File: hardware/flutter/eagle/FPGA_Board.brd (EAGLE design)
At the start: 100 x 77 mm, 45 parts, among them IC1 AT45DB161D-SU, IC2 MEGA8-AI, IC3 MAX3468CSA, Q1 8Mhz, U2 XC3S50AVQ100

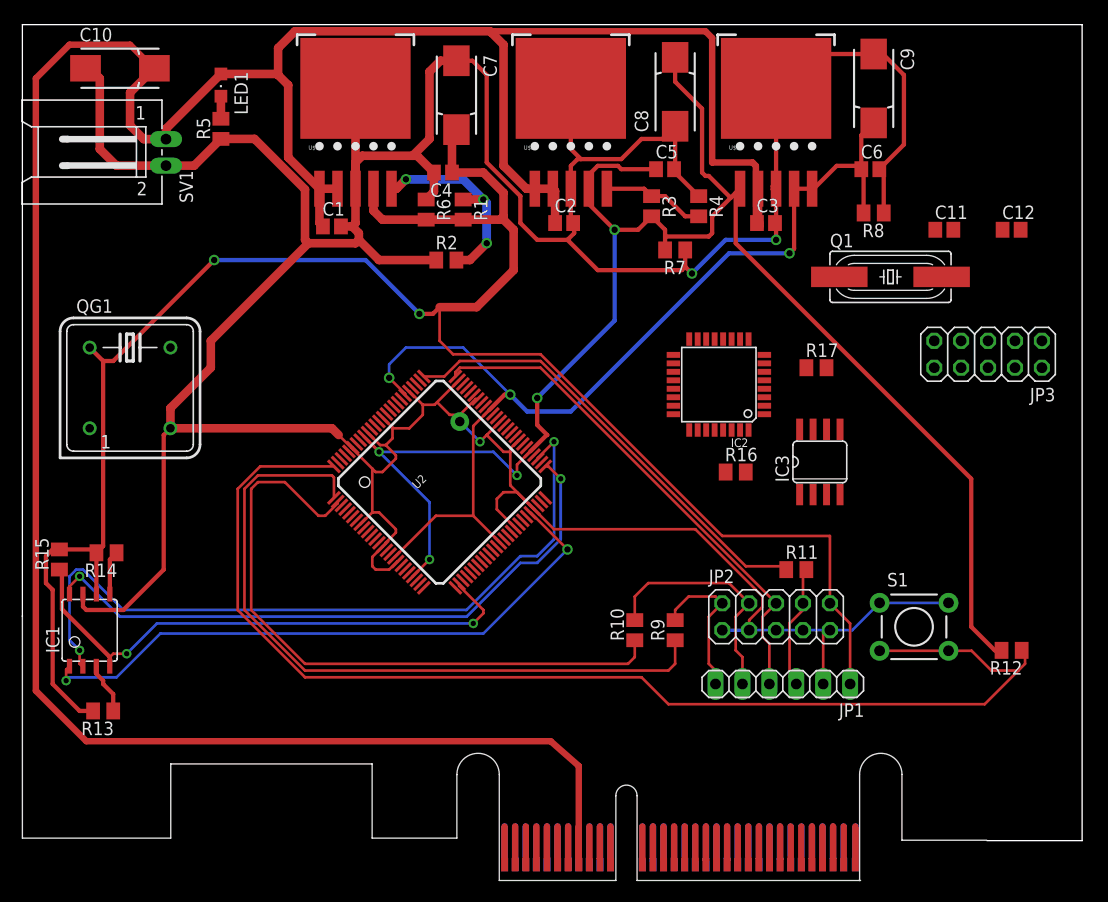
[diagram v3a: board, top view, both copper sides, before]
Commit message: organized parts of schematic by function finished routing, some power pins are not connected
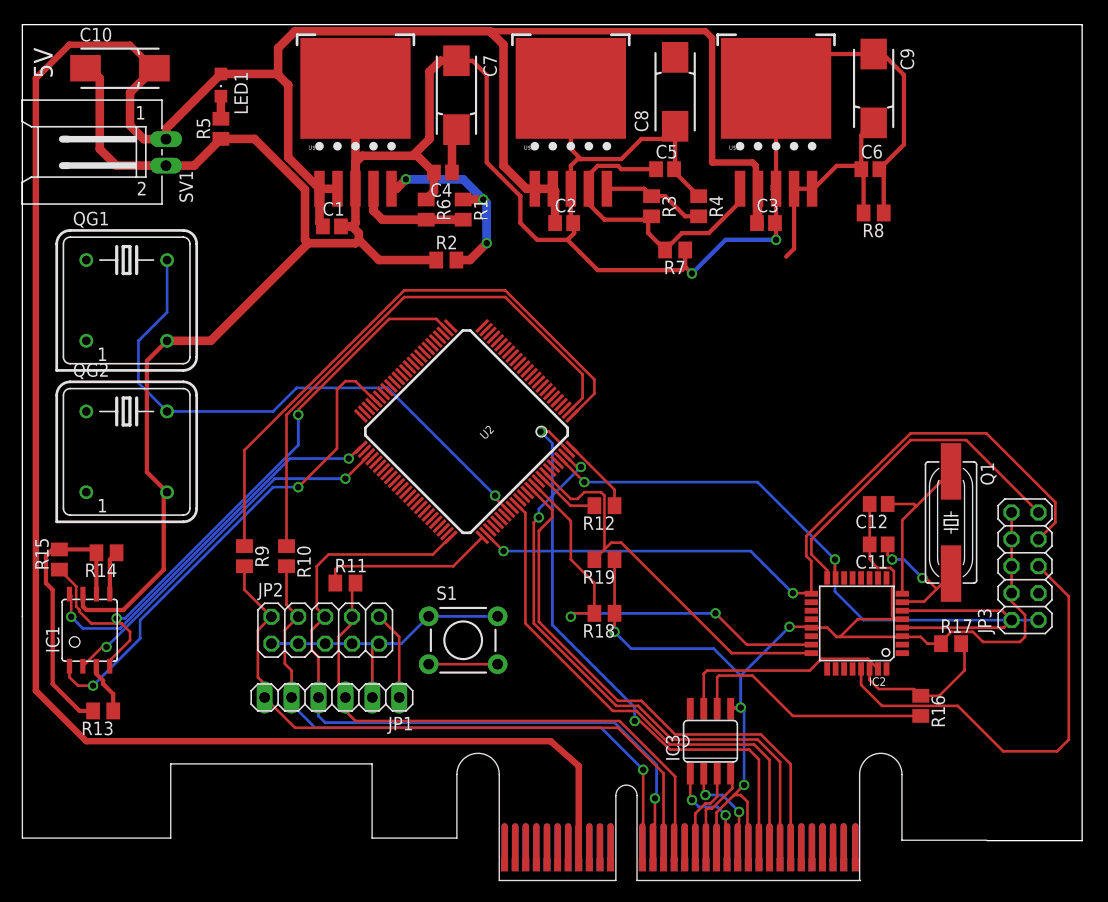
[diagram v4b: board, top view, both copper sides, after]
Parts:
- added QG2: (no value), crystal:DIL08S
- added R18, R19: 10k, resistor:M0805
- moved JP2 42.6 mm to (28.6, 22.9)
- moved R11 42.6 mm to (30.5, 27.3)
- moved S1 42.6 mm to (41.6, 21.9)
- moved JP1 42.6 mm to (29.2, 16.5)
- moved R9 41.2 mm to (21.0, 29.8), turned to 270 degrees
- moved R12 40.8 mm to (54.9, 34.6)
- moved R10 33.6 mm to (24.9, 29.8), turned to 270 degrees
- moved C11 30.3 mm to (80.8, 31.0), turned to 180 degrees
- moved R17 29.0 mm to (87.6, 21.6)
- moved C12 28.8 mm to (80.8, 34.8), turned to 180 degrees
- moved IC3 28.3 mm to (64.9, 12.4)
- moved R16 28.1 mm to (84.8, 15.7), turned to 270 degrees
- moved IC2 26.0 mm to (78.7, 23.5)
- moved Q1 23.9 mm to (87.6, 33.0), turned to 270 degrees
- moved JP3 20.3 mm to (94.6, 28.9), turned to 90 degrees
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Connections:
- removed net CLOCK: QG1.5
- new net FPGA_SPI_CLOCK: QG1.5, QG2.5, U2.P83
- new net N$13: U$4.A01(PRSNT1), U$4.A32(PRSNT2)
- new net TIMING_RESET: IC2.24, R19.2, U2.P93
- new net UC_FPGA_SPI_CS: IC2.23, R18.2, U2.P90
- new net UC_MISO: IC2.16, JP3.9
- new net UC_MOSI: IC2.15, JP3.1, U2.P97
- new net UC_RESET: IC2.29, JP3.5
- new net UC_SCK: IC2.17, JP3.7, U2.P77
- net GND: now also JP3.10, JP3.4, JP3.6, JP3.8, QG2.4, R18.1, R19.1
- net SLOWCLK/CLK: now also U2.P85
- net SLOWCLK/CS: now also U2.P98
- net SLOWCLK/MOSI: now also U2.P99
- net VCC3.3: now also JP3.2, QG2.8
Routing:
- net VCC2.5: track 160.6 -> 36.1 mm, vias 5 -> 0
- net VCC3.3: track 187.6 -> 71.1 mm, vias 2 -> 0
- net PROG_B: track 116.2 -> 13.7 mm
- net VCC1.2: track 99.6 -> 23.5 mm, vias 3 -> 0
- net UC_SCK: track 0.00 -> 73.0 mm, vias 0 -> 2
- net SLOWCLK/MOSI: track 0.00 -> 57.6 mm, vias 0 -> 2
- net SLOWCLK/CS: track 0.00 -> 56.9 mm, vias 0 -> 2
- net UC_MOSI: track 0.00 -> 54.9 mm, vias 0 -> 2
- net FPGA_SPI_CLOCK: track 0.00 -> 54.6 mm, vias 0 -> 1
- net PPS: track 0.00 -> 52.7 mm
- net SLOWCLK/CLK: track 0.00 -> 49.9 mm
- net TMS: track 14.6 -> 63.4 mm
- net TCK: track 12.2 -> 55.5 mm
- net UC_RESET: track 0.00 -> 41.7 mm
- net UC_FPGA_SPI_CS: track 0.00 -> 40.9 mm, vias 0 -> 2
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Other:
- board text added: "5V"

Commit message: connected all the signals to wires just gps module is missing on the board
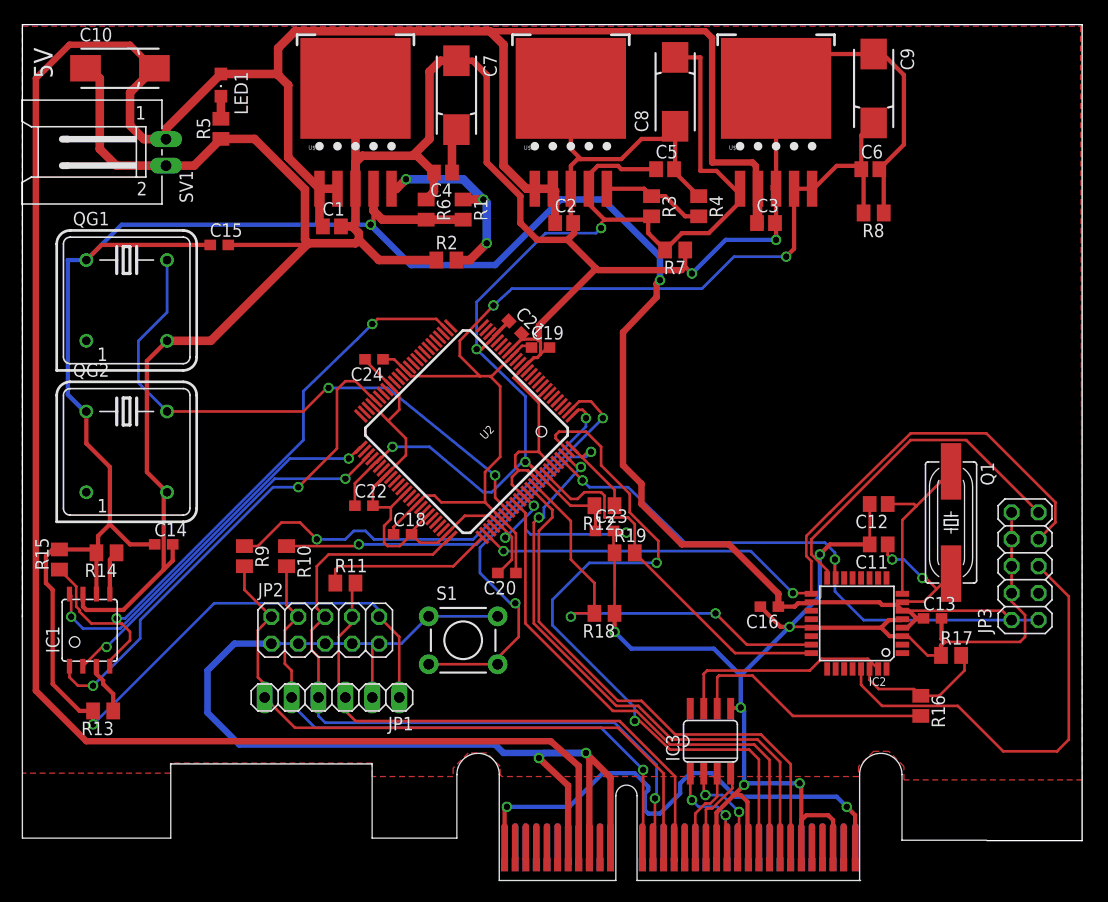
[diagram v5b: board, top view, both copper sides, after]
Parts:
- added C13, C14, C15, C16, C18, C19, C20, C21, C22, C23, C24: (no value), resistor:C0603
- moved R19 2.01 mm to (56.8, 30.2), turned to 0 degrees
- moved R17 1.11 mm to (87.6, 20.5)
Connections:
- removed net AVCC: IC2.18
- net GND: now also C13.2, C14.2, C15.2, C16.2, C18.2, C19.2, C20.2, C21.2, C22.2, C23.2, C24.2
- net VCC1.2: now also C18.1, C19.1, C20.1, C24.1
- net VCC2.5: now also C21.1, C22.1, C23.1
- net VCC3.3: now also C13.1, C14.1, C15.1, C16.1, IC2.18
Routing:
- net GND: track 409.1 -> 647.4 mm, vias 6 -> 13
- net VCC3.3: track 71.1 -> 273.7 mm, vias 0 -> 3
- net VCC2.5: track 36.1 -> 124.0 mm, vias 0 -> 4
- net VCC1.2: track 23.5 -> 109.7 mm, vias 0 -> 2
- net N$13: track 0.00 -> 51.5 mm, vias 0 -> 2
- net PROG_B: track 13.7 -> 42.5 mm, vias 0 -> 2
- net N$4: track 56.1 -> 41.8 mm, vias 0 -> 2
- net N$2: track 52.1 -> 39.4 mm, vias 0 -> 2
- net SLOWCLK/MOSI: track 57.6 -> 69.5 mm
- net TIMING_RESET: track 37.5 -> 35.4 mm
- net N$9: track 14.3 -> 13.2 mm
- net CS_EEPROM: track 60.1 -> 60.8 mm
- net FPGA_SPI_CLOCK: track 54.6 -> 55.2 mm, vias 1 -> 2
- added copper zone on layer 1, net N$14

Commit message: applied changed in hgg.lbr to the board, added ground planes
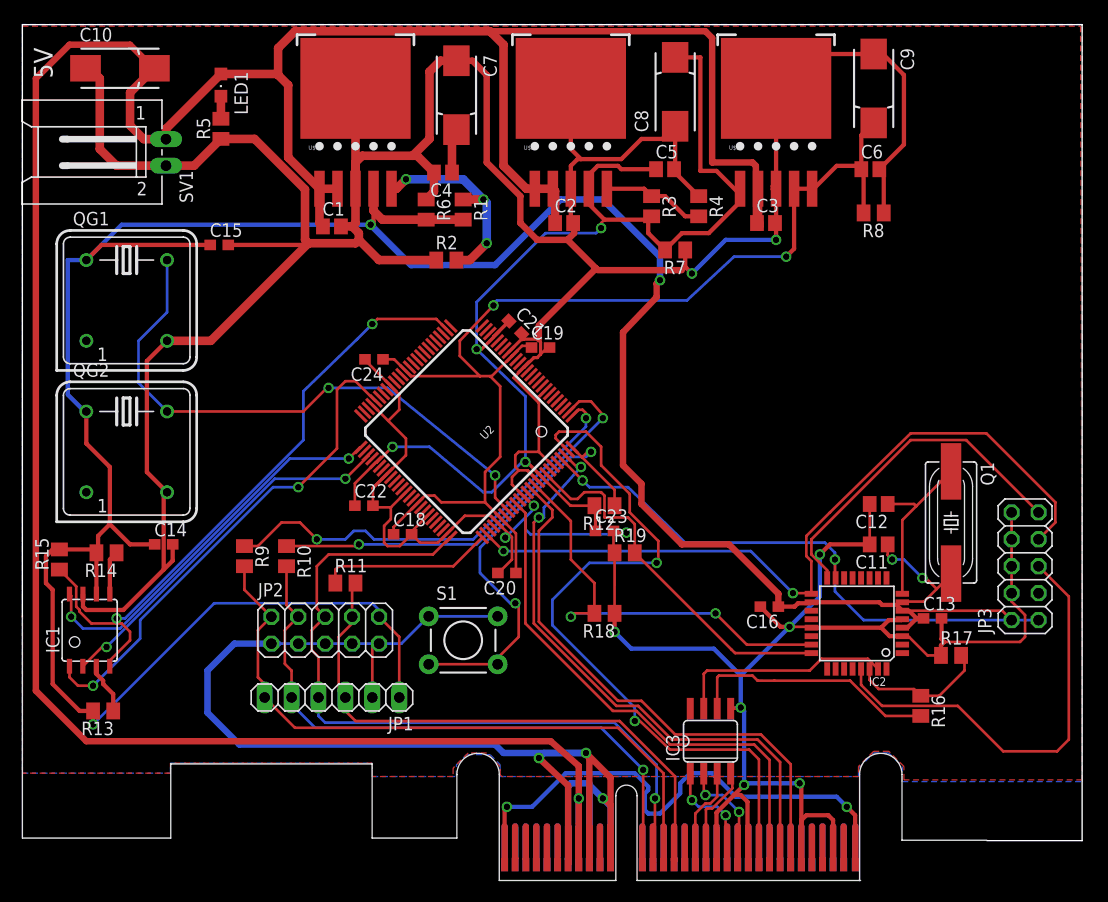
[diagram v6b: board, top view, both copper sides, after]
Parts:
- added U$5: HGG_LOGO, hgg:HGG_LOGO
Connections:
- net +5V: now also U$4.B08(+5V)
- net GND: now also U$4.B07(GND), U$4.B09(GND), U$4.B11(GND)
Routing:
- net GND: track 647.4 -> 681.4 mm, vias 13 -> 14
- net +5V: track 268.5 -> 274.7 mm, vias 0 -> 1
- added copper zone on layer 1, net GND
- added copper zone on layer 16, net GND
- removed copper zone on layer 1, net N$14
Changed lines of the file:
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@@
 <element name="C23" library="resistor" package="C0603" value="" x="54.9275" y="32.22625"/>
 <element name="C24" library="resistor" package="C0603" value="" x="33.17875" y="48.41875" rot="R180"/>
+<element name="U$5" library="hgg" package="HGG_LOGO" value="HGG_LOGO" x="90.17" y="70.96125"/>
 </elements>
 <signals>
@@
 <wire x1="53.49875" y1="10.795" x2="53.49875" y2="0.74125" width="0.6096" layer="1"/>
 <wire x1="53.49875" y1="0.74125" x2="53.5" y2="0.74" width="0.6096" layer="1"/>
-<wire x1="55.5" y1="0.74" x2="55.5" y2="8.9525" width="0.6096" layer="1"/>
+<wire x1="55.5" y1="0.74" x2="55.5" y2="6.35" width="0.6096" layer="1"/>
+<wire x1="55.5" y1="6.35" x2="55.5" y2="8.9525" width="0.6096" layer="1"/>
 <wire x1="55.5" y1="8.9525" x2="53.18125" y2="11.27125" width="0.6096" layer="1"/>
 <via x="53.18125" y="11.27125" extent="1-16" drill="0.6" shape="square"/>
@@
 <wire x1="17.4625" y1="19.05" x2="20.0025" y2="21.59" width="0.6096" layer="16"/>
 <wire x1="20.0025" y1="21.59" x2="24.13" y2="21.59" width="0.6096" layer="16"/>
-<wire x1="6.0325" y1="75.8825" x2="5.9575" y2="75.8825" width="0" layer="19" extent="1-1"/>
-<wire x1="44.8437" y1="24.1681" x2="44.87" y2="28.2575" width="0" layer="19" extent="1-1"/>
+<contactref element="U$4" pad="B07(GND)"/>
+<contactref element="U$4" pad="B09(GND)"/>
+<contactref element="U$4" pad="B11(GND)"/>
+<wire x1="51.5" y1="0.74" x2="51.5" y2="8.16125" width="0.6096" layer="16"/>
+<wire x1="51.5" y1="8.16125" x2="51.7525" y2="8.41375" width="0.6096" layer="16"/>
+<wire x1="51.7525" y1="8.41375" x2="53.49875" y2="8.41375" width="0.6096" layer="16"/>
+<wire x1="53.49875" y1="8.41375" x2="53.49875" y2="8.255" width="0.6096" layer="16"/>
+<wire x1="53.49875" y1="8.255" x2="53.49875" y2="8.09625" width="0.6096" layer="16"/>
+<wire x1="53.49875" y1="8.09625" x2="53.49875" y2="0.635" width="0.6096" layer="16"/>
+<wire x1="54.76875" y1="6.985" x2="53.49875" y2="8.255" width="0.6096" layer="16"/>
+<wire x1="55.5" y1="0.74" x2="55.5" y2="6.25375" width="0.6096" layer="16"/>
+<wire x1="55.5" y1="6.25375" x2="54.76875" y2="6.985" width="0.6096" layer="16"/>
+<via x="54.76875" y="6.985" extent="1-16" drill="0.6" shape="square"/>
+<wire x1="54.76875" y1="6.985" x2="54.865" y2="6.985" width="0.6096" layer="1"/>
+<wire x1="54.865" y1="6.985" x2="55.5" y2="6.35" width="0.6096" layer="1"/>
+<wire x1="53.5" y1="0.74" x2="53.5" y2="8.095" width="0.6096" layer="16"/>
+<wire x1="53.5" y1="8.095" x2="53.49875" y2="8.09625" width="0.6096" layer="16"/>
+<polygon width="0.254" layer="1">
+<vertex x="0" y="79.85125"/>
+<vertex x="99.85375" y="79.85125"/>
+<vertex x="100.0125" y="8.73125"/>
+<vertex x="83.185" y="8.73125"/>
+<vertex x="83.185" y="10.00125"/>
+<vertex x="81.75625" y="11.43"/>
+<vertex x="80.3275" y="11.43"/>
+<vertex x="78.89875" y="10.00125"/>
+<vertex x="78.89875" y="9.04875"/>
+<vertex x="45.24375" y="9.04875"/>
+<vertex x="45.085" y="9.2075"/>
+<vertex x="45.085" y="10.00125"/>
+<vertex x="43.815" y="11.27125"/>
+<vertex x="42.06875" y="11.27125"/>
+<vertex x="40.64" y="9.8425"/>
+<vertex x="40.64" y="9.04875"/>
+<vertex x="33.02" y="9.04875"/>
+<vertex x="33.02" y="10.31875"/>
+<vertex x="13.97" y="10.31875"/>
+<vertex x="13.97" y="9.36625"/>
+<vertex x="0" y="9.36625"/>
+</polygon>
+<polygon width="0.6096" layer="16">
+<vertex x="0" y="9.36625"/>
+<vertex x="13.97" y="9.36625"/>
+<vertex x="13.97" y="10.31875"/>
+<vertex x="32.86125" y="10.31875"/>
+<vertex x="33.02" y="10.31875"/>
+<vertex x="33.02" y="9.04875"/>
+<vertex x="40.9575" y="9.04875"/>
+<vertex x="40.9575" y="10.16"/>
+<vertex x="41.91" y="11.1125"/>
+<vertex x="44.1325" y="11.1125"/>
+<vertex x="45.085" y="10.16"/>
+<vertex x="45.085" y="9.04875"/>
+<vertex x="78.89875" y="9.04875"/>
+<vertex x="78.89875" y="9.8425"/>
+<vertex x="80.3275" y="11.27125"/>
+<vertex x="81.5975" y="11.27125"/>
+<vertex x="81.75625" y="11.27125"/>
+<vertex x="83.02625" y="10.00125"/>
+<vertex x="83.02625" y="8.5725"/>
+<vertex x="100.0125" y="8.5725"/>
+<vertex x="100.0125" y="80.01"/>
+<vertex x="0" y="80.01"/>
+</polygon>
 </signal>
 <signal name="+5V">
@@
 <wire x1="69.42" y1="61.38" x2="69.3175" y2="61.2775" width="0.8128" layer="1"/>
 <contactref element="U$4" pad="A08(+5V)"/>
-<wire x1="52.5" y1="0.74" x2="52.5" y2="10.0475" width="0.6096" layer="1"/>
+<wire x1="52.5" y1="0.74" x2="52.5" y2="4.60375" width="0.6096" layer="1"/>
+<wire x1="52.5" y1="6.985" x2="52.5" y2="10.0475" width="0.6096" layer="1"/>
 <wire x1="52.5" y1="10.0475" x2="49.8475" y2="12.3825" width="0.6096" layer="1"/>
 <wire x1="49.8475" y1="12.3825" x2="6.0325" y2="12.3825" width="0.6096" layer="1"/>
@@
 <wire x1="64.4525" y1="79.375" x2="44.45" y2="79.375" width="0.6096" layer="1"/>
 <wire x1="44.45" y1="79.375" x2="44.29125" y2="79.21625" width="0.6096" layer="1"/>
+<contactref element="U$4" pad="B08(+5V)"/>
+<wire x1="52.5" y1="0.74" x2="52.5" y2="6.985" width="0.6096" layer="16"/>
+<via x="52.5" y="6.985" extent="1-16" drill="0.6" shape="square"/>
+<wire x1="52.5" y1="6.985" x2="52.5" y2="4.60375" width="0.6096" layer="1"/>
 <wire x1="12.3825" y1="75.8825" x2="12.4575" y2="75.8825" width="0" layer="19" extent="1-1"/>
 </signal>
@@
 <via x="72.0725" y="58.1025" extent="1-16" drill="0.6" shape="square"/>
 <wire x1="72.0725" y1="58.1025" x2="67.15125" y2="58.1025" width="0.254" layer="16"/>
-<wire x1="67.15125" y1="58.1025" x2="64.135" y2="55.08625" width="0.254" layer="16"/>
-<wire x1="64.135" y1="55.08625" x2="46.19625" y2="55.08625" width="0.254" layer="16"/>
-<wire x1="46.19625" y1="55.08625" x2="44.45" y2="53.49875" width="0.254" layer="16"/>
+<wire x1="67.15125" y1="58.1025" x2="62.70625" y2="53.975" width="0.254" layer="16"/>
+<wire x1="62.70625" y1="53.975" x2="44.7675" y2="53.975" width="0.254" layer="16"/>
+<wire x1="44.7675" y1="53.975" x2="44.45" y2="53.49875" width="0.254" layer="16"/>
 <via x="44.45" y="53.49875" extent="1-16" drill="0.6" shape="octagon"/>
 </signal>
@@
 <contactref element="R16" pad="2"/>
 <contactref element="IC3" pad="6"/>
-<wire x1="84.7725" y1="14.76625" x2="72.705" y2="14.76625" width="0.254" layer="1"/>
-<wire x1="72.705" y1="14.76625" x2="68.8975" y2="18.57375" width="0.254" layer="1"/>
+<wire x1="84.7725" y1="14.76625" x2="81.43625" y2="14.76625" width="0.254" layer="1"/>
+<wire x1="81.43625" y1="14.76625" x2="78.105" y2="18.0975" width="0.254" layer="1"/>
+<wire x1="78.105" y1="18.0975" x2="70.96125" y2="18.0975" width="0.254" layer="1"/>
+<wire x1="70.96125" y1="18.0975" x2="69.37125" y2="18.1" width="0.254" layer="1"/>
+<wire x1="69.37125" y1="18.1" x2="68.8975" y2="18.57375" width="0.254" layer="1"/>
 <wire x1="68.8975" y1="18.57375" x2="65.7225" y2="18.57375" width="0.254" layer="1"/>
 <wire x1="65.7225" y1="18.57375" x2="65.56375" y2="18.415" width="0.254" layer="1"/>
@@
 <wire x1="45.5" y1="5.97125" x2="45.72" y2="6.19125" width="0.4064" layer="1"/>
 <via x="45.72" y="6.19125" extent="1-16" drill="0.6" shape="square"/>
-<wire x1="45.72" y1="6.19125" x2="51.59375" y2="6.19125" width="0.4064" layer="16"/>
-<wire x1="51.59375" y1="6.19125" x2="54.76875" y2="9.36625" width="0.4064" layer="16"/>
-<wire x1="54.76875" y1="9.36625" x2="57.785" y2="9.36625" width="0.4064" layer="16"/>
+<wire x1="45.72" y1="6.19125" x2="48.10125" y2="6.19125" width="0.4064" layer="16"/>
+<wire x1="48.10125" y1="6.19125" x2="51.27625" y2="9.36625" width="0.4064" layer="16"/>
+<wire x1="51.27625" y1="9.36625" x2="57.785" y2="9.36625" width="0.4064" layer="16"/>
 <wire x1="57.785" y1="9.36625" x2="59.055" y2="8.09625" width="0.4064" layer="16"/>
 <wire x1="59.055" y1="8.09625" x2="59.055" y2="7.77875" width="0.4064" layer="16"/>
@@
 <wire x1="66.935" y1="21.01" x2="57.7825" y2="30.1625" width="0.254" layer="1"/>
 </signal>
-<signal name="N$14">
-<polygon width="0.254" layer="1">
-<vertex x="0" y="79.85125"/>
-<vertex x="99.85375" y="79.85125"/>
-<vertex x="100.0125" y="8.73125"/>
-<vertex x="83.185" y="8.73125"/>
-<vertex x="83.185" y="10.00125"/>
-<vertex x="81.75625" y="11.43"/>
-<vertex x="80.3275" y="11.43"/>
-<vertex x="78.89875" y="10.00125"/>
-<vertex x="78.89875" y="9.04875"/>
-<vertex x="45.24375" y="9.04875"/>
-<vertex x="45.085" y="9.2075"/>
-<vertex x="45.085" y="10.00125"/>
-<vertex x="43.815" y="11.27125"/>
-<vertex x="42.06875" y="11.27125"/>
-<vertex x="40.64" y="9.8425"/>
-<vertex x="40.64" y="9.04875"/>
-<vertex x="33.02" y="9.04875"/>
-<vertex x="33.02" y="10.31875"/>
-<vertex x="13.97" y="10.31875"/>
-<vertex x="13.97" y="9.36625"/>
-<vertex x="0" y="9.36625"/>
-</polygon>
-</signal>
 </signals>
